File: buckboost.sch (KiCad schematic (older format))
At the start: 16 parts

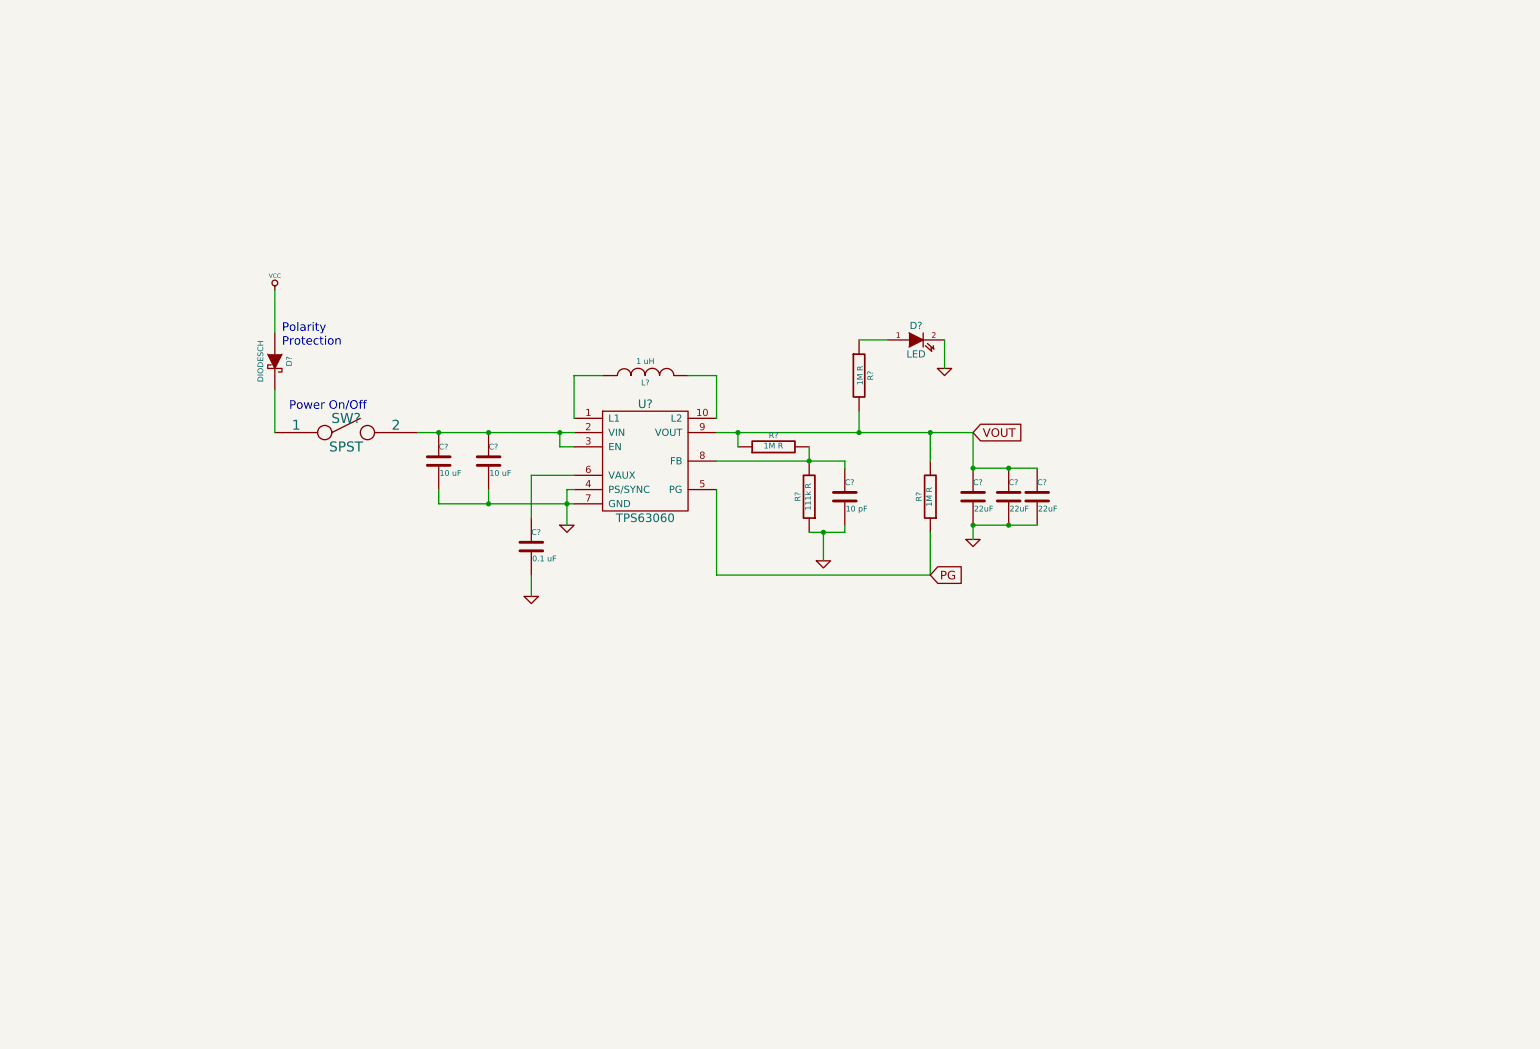
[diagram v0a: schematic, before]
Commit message: Added output control via 0.1" Header.
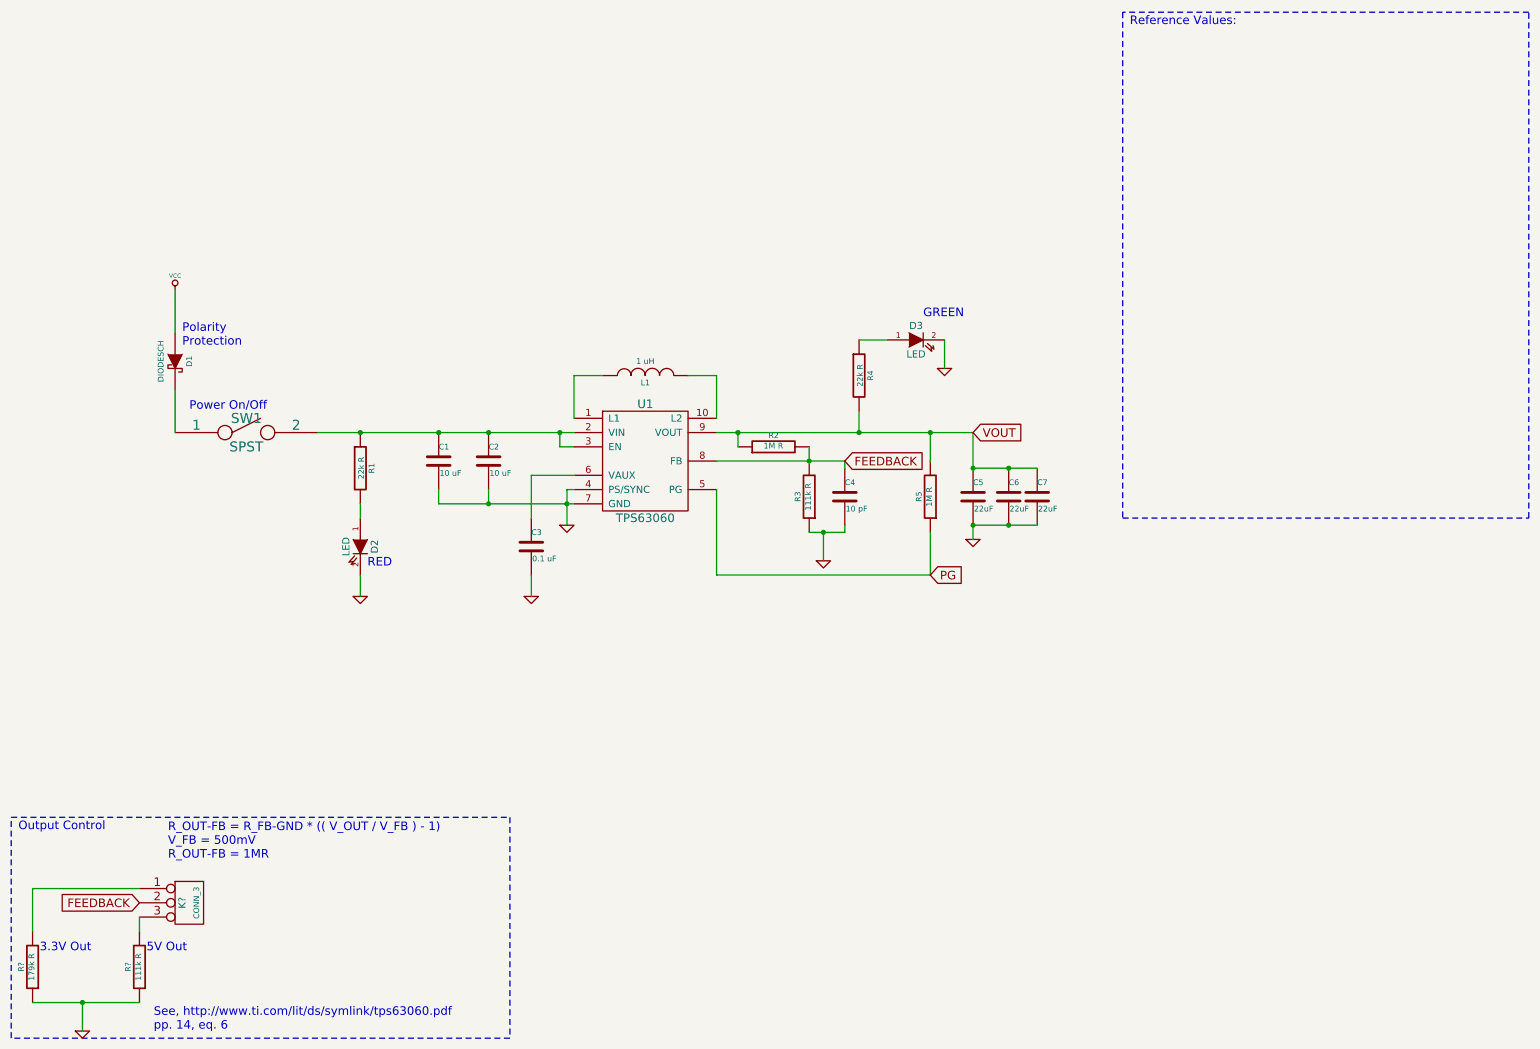
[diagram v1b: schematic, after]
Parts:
- added D2: LED, symbol LED
- added K?: CONN_3, symbol CONN_3
- added R1: 22k R, symbol R
- added R?: 111k R, symbol R
- added R?: 179k R, symbol R
- R4: renamed from R?; value 1M R -> 22k R
- gave numbers to parts that had none: 15
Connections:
- net GND: now also D2.2 (K), R?.1, R?.1
- net at C1.1, C2.1, SW1.2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: now also R1.1
- net FEEDBACK: now reaches C4.1, R2.2, R3.2, U1.8 (FB)
- net FEEDBACK: now also K?.2 (PM)
- new net: D2.1 (A), R1.2
- new net: K?.1 (P1), R?.2
- new net: K?.3 (P3), R?.2
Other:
- note added: "3.3V Out"
- note added: "5V Out"
- note added: "GREEN"
- note added: "Output Control"
- note added: "RED"
- note added: "R_OUT-FB = R_FB-GND * (( V_OUT / V_FB ) - 1)\nV_FB = 500mV\nR_OUT-FB = 1MR"
- note added: "Reference Values:\n"
- note added: "See, http://www.ti.com/lit/ds/symlink/tps63060.pdf\npp. 14, eq. 6"
- moved on the sheet: D1, SW1

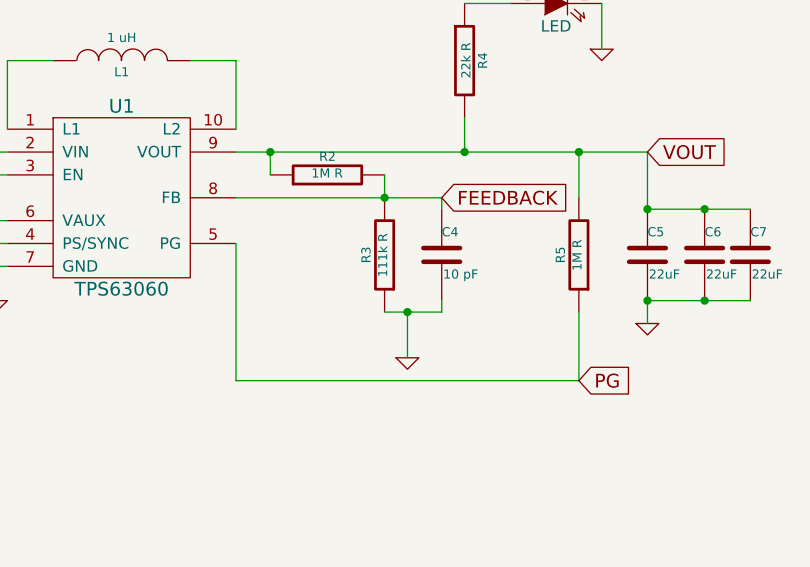
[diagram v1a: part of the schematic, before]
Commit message: Removed redundant feedback resistor.
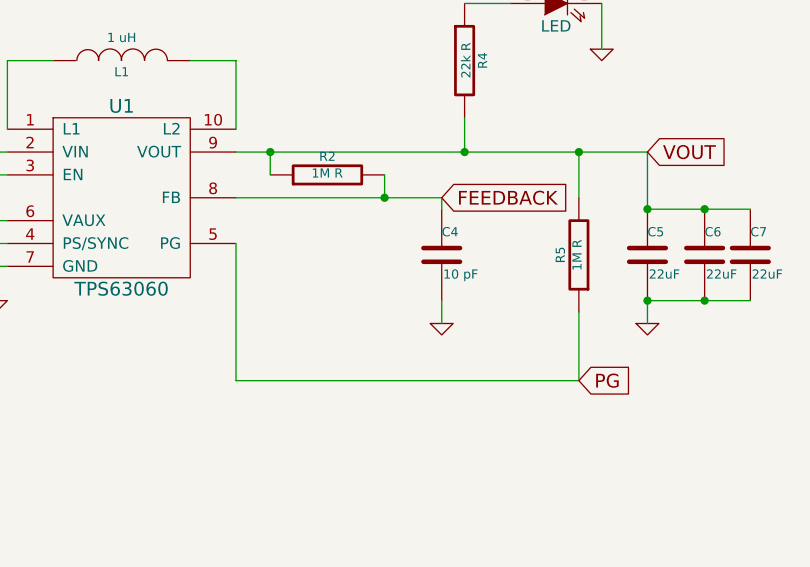
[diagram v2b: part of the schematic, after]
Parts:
- removed R3: 111k R, symbol R
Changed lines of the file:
@@
 L GND #PWR5
 U 1 1 56ED0DD5
-P 6200 4400
-F 0 "#PWR5" H 6200 4400 30  0001 C CNN
-F 1 "GND" H 6200 4330 30  0001 C CNN
-F 2 "" H 6200 4400 60  0000 C CNN
-F 3 "" H 6200 4400 60  0000 C CNN
-	1    6200 4400
+P 6350 4250
+F 0 "#PWR5" H 6350 4250 30  0001 C CNN
+F 1 "GND" H 6350 4180 30  0001 C CNN
+F 2 "" H 6350 4250 60  0000 C CNN
+F 3 "" H 6350 4250 60  0000 C CNN
+	1    6350 4250
 	1    0    0    -1
 $EndComp
@@
 	6350 3700 6350 3750
 Wire Wire Line
-	6350 4200 6350 4150
+	6350 4150 6350 4250
 Connection ~ 5600 3500
 Wire Wire Line
@@
 Wire Notes Line
 	11150 4100 11150 550
-Wire Wire Line
-	6200 4200 6200 4400
-Connection ~ 6200 4200
-Wire Wire Line
-	6100 4200 6350 4200
-$Comp
-L R R3
-U 1 1 56ED05AE
-P 6100 3950
-F 0 "R3" V 6180 3950 40  0000 C CNN
-F 1 "111k R" V 6107 3951 40  0000 C CNN
-F 2 "" V 6030 3950 30  0000 C CNN
-F 3 "" H 6100 3950 30  0000 C CNN
-	1    6100 3950
-	-1   0    0    1
-$EndComp
 Text GLabel 1400 6800 0    60   Input ~ 0
 FEEDBACK
